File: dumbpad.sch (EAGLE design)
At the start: 44 parts

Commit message: updated readme, made jumpers a little bigger for easier soldering, updated version to 1.0
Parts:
- JP1, JP2: value JUMPER-SMT_3_NO_NO-SILK -> JUMPER-SMT_3_NO_NO_SILK; device SparkFun-Jumpers:JUMPER-SMT_3_NO_NO-SILK -> SparkFun-Jumpers:JUMPER-SMT_3_NO_NO_SILK
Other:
- note added: "Date: April 28, 2020"
- note added: "Rev: 1.0"
- note removed: "Date: April 21, 2020"
- note removed: "Rev: 0.8"
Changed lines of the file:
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@@
 <part name="S17" library="SparkFun-Switches" deviceset="MOMENTARY-SWITCH-SPST" device="-PTH-6.0MM"/>
 <part name="GND4" library="supply1" library_urn="urn:adsk.eagle:library:371" deviceset="GND" device=""/>
-<part name="JP1" library="SparkFun-Jumpers" deviceset="JUMPER-SMT_3_NO" device="_NO-SILK"/>
-<part name="JP2" library="SparkFun-Jumpers" deviceset="JUMPER-SMT_3_NO" device="_NO-SILK"/>
+<part name="JP1" library="SparkFun-Jumpers" deviceset="JUMPER-SMT_3_NO" device="_NO_SILK" value="JUMPER-SMT_3_NO_NO_SILK"/>
+<part name="JP2" library="SparkFun-Jumpers" deviceset="JUMPER-SMT_3_NO" device="_NO_SILK" value="JUMPER-SMT_3_NO_NO_SILK"/>
 <part name="D20" library="SparkFun-LED" deviceset="LED" device="3MM"/>
 <part name="R3" library="SparkFun-Resistors" deviceset="330OHM" device="-HORIZ-1/10W-5%" value="330"/>
@@
 <wire x1="0" y1="172.72" x2="0" y2="0" width="0.1524" layer="97"/>
 <text x="307.34" y="2.54" size="1.778" layer="97">Rev:
-0.8</text>
+1.0</text>
 <text x="279.4" y="2.54" size="1.778" layer="97">Date:
-April 21, 2020</text>
+April 28, 2020</text>
 <text x="279.4" y="10.16" size="1.778" layer="97">Design By:
 github.com/imchipwood</text>

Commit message: swapped some LED pins to make the first two LEDs connecting to the same pins as v0.x PCBs
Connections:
- net LED0: now also B1.12(MISO); no longer B1.13(SCK)
- net LED1: now also B1.13(SCK); no longer B1.12(MISO)
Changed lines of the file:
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@@
 </segment>
 <segment>
-<pinref part="B1" gate="G$1" pin="13(SCK)"/>
-<wire x1="294.64" y1="132.08" x2="302.26" y2="132.08" width="0.1524" layer="91"/>
-<label x="302.26" y="132.08" size="1.778" layer="95"/>
+<pinref part="B1" gate="G$1" pin="12(MISO)"/>
+<wire x1="294.64" y1="129.54" x2="302.26" y2="129.54" width="0.1524" layer="91"/>
+<label x="302.26" y="129.54" size="1.778" layer="95"/>
 </segment>
 </net>
@@
 </segment>
 <segment>
-<pinref part="B1" gate="G$1" pin="12(MISO)"/>
-<wire x1="294.64" y1="129.54" x2="302.26" y2="129.54" width="0.1524" layer="91"/>
-<label x="302.26" y="129.54" size="1.778" layer="95"/>
+<pinref part="B1" gate="G$1" pin="13(SCK)"/>
+<wire x1="294.64" y1="132.08" x2="302.26" y2="132.08" width="0.1524" layer="91"/>
+<label x="302.26" y="132.08" size="1.778" layer="95"/>
 </segment>
 </net>

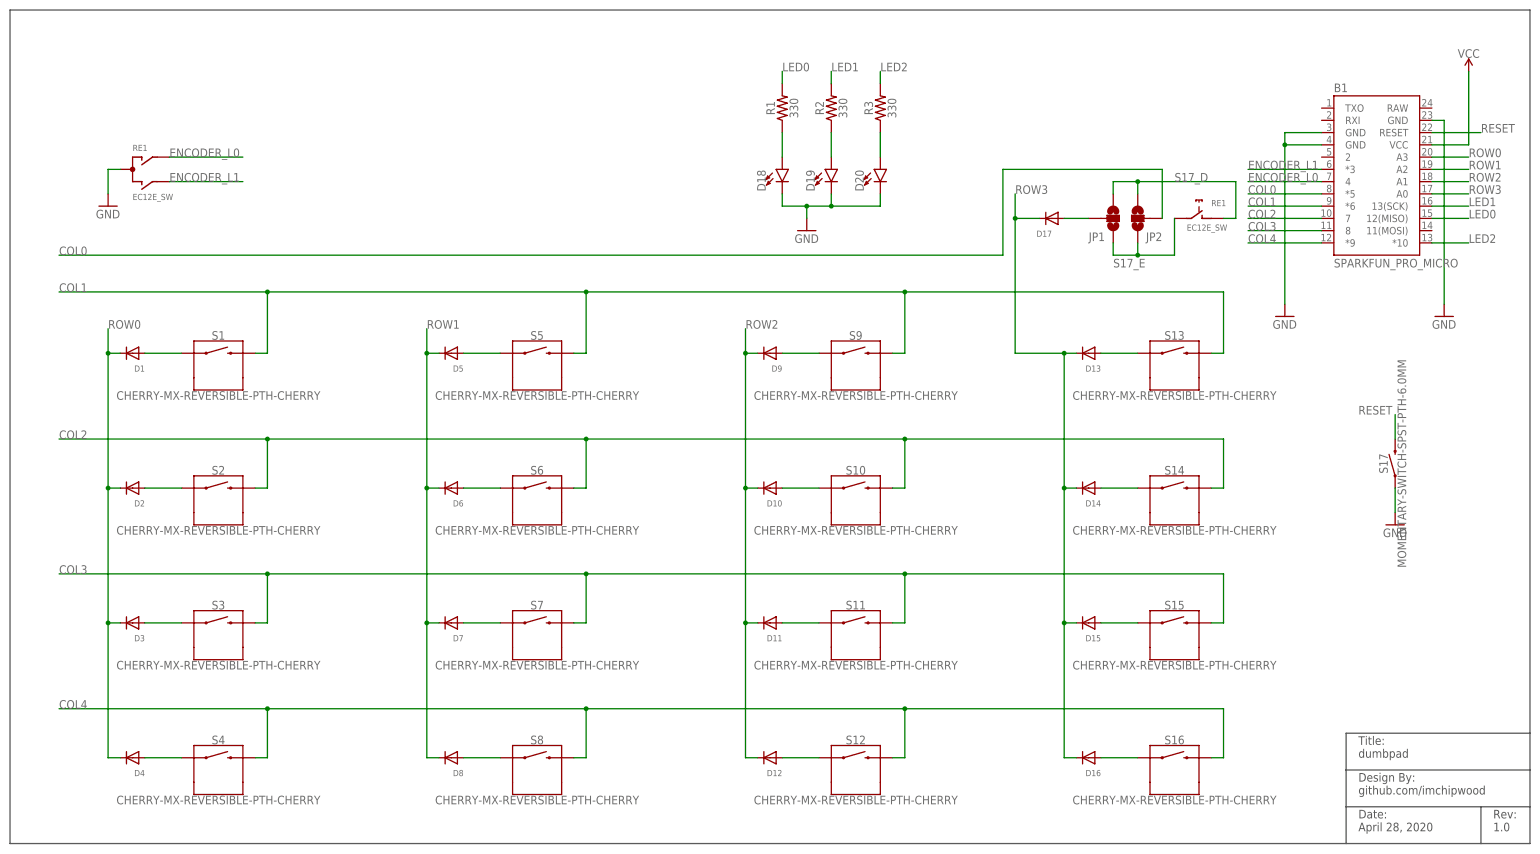
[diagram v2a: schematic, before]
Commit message: all parts have bottom silk screen now, rerouted some stuff
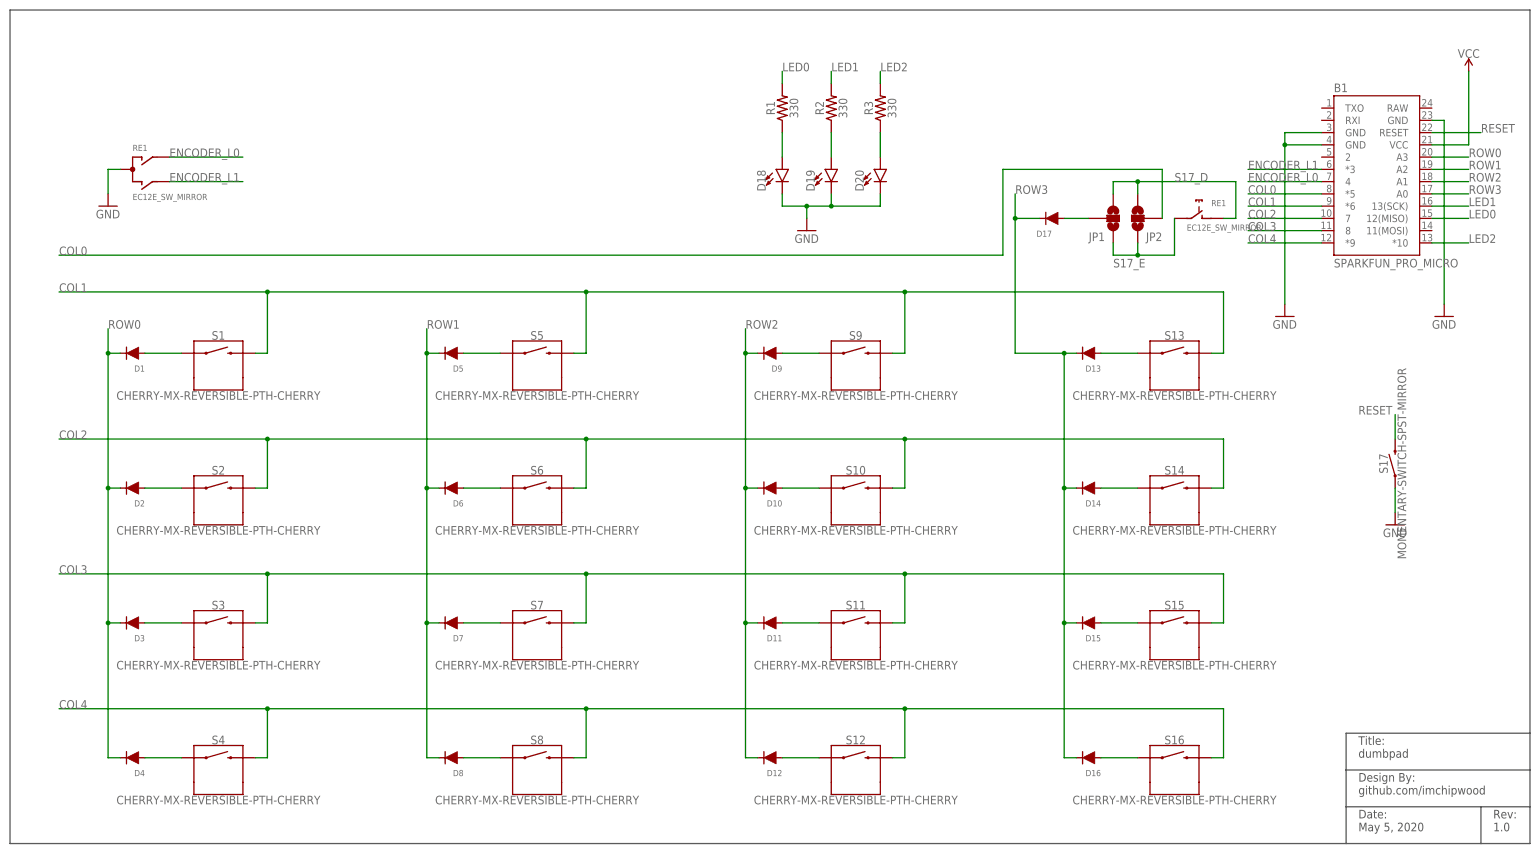
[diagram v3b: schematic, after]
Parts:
- D1, D10, D11, D12, D13, D14, D15, D16, D17, D2, D3, D4, D5, D6, D7, D8, D9: value (none) -> DO-1N4148_MIRROR; device adafruit:DIODEDO-1N4148 -> cpwood:DO-1N4148_MIRROR
- JP1: device SparkFun-Jumpers:JUMPER-SMT_3_NO_NO_SILK -> cpwood:JUMPER-SMT_3_NO_NO_SILK
- R1, R2, R3: device SparkFun-Resistors:330OHM-HORIZ-1/10W-5% -> cpwood:RESISTOR_MIRROR
- RE1: value EC12E_SW -> EC12E_SW_MIRROR; device switch-alps:EC12E_SW -> cpwood:EC12E_SW_MIRROR
- S17: value MOMENTARY-SWITCH-SPST-PTH-6.0MM -> MOMENTARY-SWITCH-SPST-MIRROR; device SparkFun-Switches:MOMENTARY-SWITCH-SPST-PTH-6.0MM -> cpwood:MOMENTARY-SWITCH-SPST-MIRROR
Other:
- note added: "Date: May 5, 2020"
- note removed: "Date: April 28, 2020"
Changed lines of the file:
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@@
 <part name="S1" library="cpwood" deviceset="CHERRY-MX-REVERSIBLE" device="-PTH-CHERRY"/>
 <part name="B1" library="SparkFun-Boards" deviceset="SPARKFUN_PRO_MICRO" device=""/>
-<part name="RE1" library="switch-alps" library_urn="urn:adsk.eagle:library:373" deviceset="EC12E_SW" device="" package3d_urn="urn:adsk.eagle:package:27083/1"/>
+<part name="RE1" library="cpwood" deviceset="EC12E_SW_MIRROR" device="" package3d_urn="urn:adsk.eagle:package:27083/1"/>
 <part name="GND1" library="supply1" library_urn="urn:adsk.eagle:library:371" deviceset="GND" device=""/>
 <part name="S2" library="cpwood" deviceset="CHERRY-MX-REVERSIBLE" device="-PTH-CHERRY"/>
@@
 <part name="GND3" library="supply1" library_urn="urn:adsk.eagle:library:371" deviceset="GND" device=""/>
 <part name="SUPPLY2" library="SparkFun-PowerSymbols" deviceset="VCC" device=""/>
-<part name="D1" library="adafruit" deviceset="DIODE" device="DO-1N4148"/>
-<part name="D2" library="adafruit" deviceset="DIODE" device="DO-1N4148"/>
-<part name="D3" library="adafruit" deviceset="DIODE" device="DO-1N4148"/>
-<part name="D4" library="adafruit" deviceset="DIODE" device="DO-1N4148"/>
-<part name="D5" library="adafruit" deviceset="DIODE" device="DO-1N4148"/>
-<part name="D6" library="adafruit" deviceset="DIODE" device="DO-1N4148"/>
-<part name="D7" library="adafruit" deviceset="DIODE" device="DO-1N4148"/>
-<part name="D8" library="adafruit" deviceset="DIODE" device="DO-1N4148"/>
-<part name="D9" library="adafruit" deviceset="DIODE" device="DO-1N4148"/>
-<part name="D10" library="adafruit" deviceset="DIODE" device="DO-1N4148"/>
-<part name="D11" library="adafruit" deviceset="DIODE" device="DO-1N4148"/>
-<part name="D12" library="adafruit" deviceset="DIODE" device="DO-1N4148"/>
-<part name="D13" library="adafruit" deviceset="DIODE" device="DO-1N4148"/>
-<part name="D14" library="adafruit" deviceset="DIODE" device="DO-1N4148"/>
-<part name="D15" library="adafruit" deviceset="DIODE" device="DO-1N4148"/>
-<part name="D16" library="adafruit" deviceset="DIODE" device="DO-1N4148"/>
-<part name="D17" library="adafruit" deviceset="DIODE" device="DO-1N4148"/>
+<part name="D1" library="cpwood" deviceset="DO-1N4148_MIRROR" device=""/>
+<part name="D2" library="cpwood" deviceset="DO-1N4148_MIRROR" device=""/>
+<part name="D3" library="cpwood" deviceset="DO-1N4148_MIRROR" device=""/>
+<part name="D4" library="cpwood" deviceset="DO-1N4148_MIRROR" device=""/>
+<part name="D5" library="cpwood" deviceset="DO-1N4148_MIRROR" device=""/>
+<part name="D6" library="cpwood" deviceset="DO-1N4148_MIRROR" device=""/>
+<part name="D7" library="cpwood" deviceset="DO-1N4148_MIRROR" device=""/>
+<part name="D8" library="cpwood" deviceset="DO-1N4148_MIRROR" device=""/>
+<part name="D9" library="cpwood" deviceset="DO-1N4148_MIRROR" device=""/>
+<part name="D10" library="cpwood" deviceset="DO-1N4148_MIRROR" device=""/>
+<part name="D11" library="cpwood" deviceset="DO-1N4148_MIRROR" device=""/>
+<part name="D12" library="cpwood" deviceset="DO-1N4148_MIRROR" device=""/>
+<part name="D13" library="cpwood" deviceset="DO-1N4148_MIRROR" device=""/>
+<part name="D14" library="cpwood" deviceset="DO-1N4148_MIRROR" device=""/>
+<part name="D15" library="cpwood" deviceset="DO-1N4148_MIRROR" device=""/>
+<part name="D16" library="cpwood" deviceset="DO-1N4148_MIRROR" device=""/>
+<part name="D17" library="cpwood" deviceset="DO-1N4148_MIRROR" device=""/>
 <part name="D18" library="SparkFun-LED" deviceset="LED" device="3MM"/>
 <part name="D19" library="SparkFun-LED" deviceset="LED" device="3MM"/>
-<part name="R1" library="SparkFun-Resistors" deviceset="330OHM" device="-HORIZ-1/10W-5%" value="330"/>
-<part name="R2" library="SparkFun-Resistors" deviceset="330OHM" device="-HORIZ-1/10W-5%" value="330"/>
+<part name="R1" library="cpwood" deviceset="RESISTOR_MIRROR" device="" value="330"/>
+<part name="R2" library="cpwood" deviceset="RESISTOR_MIRROR" device="" value="330"/>
 <part name="GND2" library="supply1" library_urn="urn:adsk.eagle:library:371" deviceset="GND" device=""/>
-<part name="S17" library="SparkFun-Switches" deviceset="MOMENTARY-SWITCH-SPST" device="-PTH-6.0MM"/>
+<part name="S17" library="cpwood" deviceset="MOMENTARY-SWITCH-SPST-MIRROR" device=""/>
 <part name="GND4" library="supply1" library_urn="urn:adsk.eagle:library:371" deviceset="GND" device=""/>
-<part name="JP1" library="SparkFun-Jumpers" deviceset="JUMPER-SMT_3_NO" device="_NO_SILK" value="JUMPER-SMT_3_NO_NO_SILK"/>
+<part name="JP1" library="cpwood" deviceset="JUMPER-SMT_3_NO" device="_NO_SILK" value="JUMPER-SMT_3_NO_NO_SILK"/>
 <part name="JP2" library="SparkFun-Jumpers" deviceset="JUMPER-SMT_3_NO" device="_NO_SILK" value="JUMPER-SMT_3_NO_NO_SILK"/>
 <part name="D20" library="SparkFun-LED" deviceset="LED" device="3MM"/>
-<part name="R3" library="SparkFun-Resistors" deviceset="330OHM" device="-HORIZ-1/10W-5%" value="330"/>
+<part name="R3" library="cpwood" deviceset="RESISTOR_MIRROR" device="" value="330"/>
 </parts>
 <sheets>
@@
 1.0</text>
 <text x="279.4" y="2.54" size="1.778" layer="97">Date:
-April 28, 2020</text>
+May 5, 2020</text>
 <text x="279.4" y="10.16" size="1.778" layer="97">Design By:
 github.com/imchipwood</text>
@@
 <instance part="D1" gate="G$1" x="25.4" y="101.6" smashed="yes" rot="R180">
 <attribute name="NAME" x="27.94" y="99.06" size="1.27" layer="95" rot="R180"/>
-<attribute name="VALUE" x="27.94" y="105.41" size="1.27" layer="96" rot="R180"/>
 </instance>
 <instance part="D2" gate="G$1" x="25.4" y="73.66" smashed="yes" rot="R180">
 <attribute name="NAME" x="27.94" y="71.12" size="1.27" layer="95" rot="R180"/>
-<attribute name="VALUE" x="27.94" y="77.47" size="1.27" layer="96" rot="R180"/>
 </instance>
 <instance part="D3" gate="G$1" x="25.4" y="45.72" smashed="yes" rot="R180">
 <attribute name="NAME" x="27.94" y="43.18" size="1.27" layer="95" rot="R180"/>
-<attribute name="VALUE" x="27.94" y="49.53" size="1.27" layer="96" rot="R180"/>
 </instance>
 <instance part="D4" gate="G$1" x="25.4" y="17.78" smashed="yes" rot="R180">
 <attribute name="NAME" x="27.94" y="15.24" size="1.27" layer="95" rot="R180"/>
-<attribute name="VALUE" x="27.94" y="21.59" size="1.27" layer="96" rot="R180"/>
 </instance>
 <instance part="D5" gate="G$1" x="91.44" y="101.6" smashed="yes" rot="R180">
 <attribute name="NAME" x="93.98" y="99.06" size="1.27" layer="95" rot="R180"/>
-<attribute name="VALUE" x="93.98" y="105.41" size="1.27" layer="96" rot="R180"/>
 </instance>
 <instance part="D6" gate="G$1" x="91.44" y="73.66" smashed="yes" rot="R180">
 <attribute name="NAME" x="93.98" y="71.12" size="1.27" layer="95" rot="R180"/>
-<attribute name="VALUE" x="93.98" y="77.47" size="1.27" layer="96" rot="R180"/>
 </instance>
 <instance part="D7" gate="G$1" x="91.44" y="45.72" smashed="yes" rot="R180">
 <attribute name="NAME" x="93.98" y="43.18" size="1.27" layer="95" rot="R180"/>
-<attribute name="VALUE" x="93.98" y="49.53" size="1.27" layer="96" rot="R180"/>
 </instance>
 <instance part="D8" gate="G$1" x="91.44" y="17.78" smashed="yes" rot="R180">
 <attribute name="NAME" x="93.98" y="15.24" size="1.27" layer="95" rot="R180"/>
-<attribute name="VALUE" x="93.98" y="21.59" size="1.27" layer="96" rot="R180"/>
 </instance>
 <instance part="D9" gate="G$1" x="157.48" y="101.6" smashed="yes" rot="R180">
 <attribute name="NAME" x="160.02" y="99.06" size="1.27" layer="95" rot="R180"/>
-<attribute name="VALUE" x="160.02" y="105.41" size="1.27" layer="96" rot="R180"/>
 </instance>
 <instance part="D10" gate="G$1" x="157.48" y="73.66" smashed="yes" rot="R180">
 <attribute name="NAME" x="160.02" y="71.12" size="1.27" layer="95" rot="R180"/>
-<attribute name="VALUE" x="160.02" y="77.47" size="1.27" layer="96" rot="R180"/>
 </instance>
 <instance part="D11" gate="G$1" x="157.48" y="45.72" smashed="yes" rot="R180">
 <attribute name="NAME" x="160.02" y="43.18" size="1.27" layer="95" rot="R180"/>
-<attribute name="VALUE" x="160.02" y="49.53" size="1.27" layer="96" rot="R180"/>
 </instance>
 <instance part="D12" gate="G$1" x="157.48" y="17.78" smashed="yes" rot="R180">
 <attribute name="NAME" x="160.02" y="15.24" size="1.27" layer="95" rot="R180"/>
-<attribute name="VALUE" x="160.02" y="21.59" size="1.27" layer="96" rot="R180"/>
 </instance>
 <instance part="D13" gate="G$1" x="223.52" y="101.6" smashed="yes" rot="R180">
 <attribute name="NAME" x="226.06" y="99.06" size="1.27" layer="95" rot="R180"/>
-<attribute name="VALUE" x="226.06" y="105.41" size="1.27" layer="96" rot="R180"/>
 </instance>
 <instance part="D14" gate="G$1" x="223.52" y="73.66" smashed="yes" rot="R180">
 <attribute name="NAME" x="226.06" y="71.12" size="1.27" layer="95" rot="R180"/>
-<attribute name="VALUE" x="226.06" y="77.47" size="1.27" layer="96" rot="R180"/>
 </instance>
 <instance part="D15" gate="G$1" x="223.52" y="45.72" smashed="yes" rot="R180">
 <attribute name="NAME" x="226.06" y="43.18" size="1.27" layer="95" rot="R180"/>
-<attribute name="VALUE" x="226.06" y="49.53" size="1.27" layer="96" rot="R180"/>
 </instance>
 <instance part="D16" gate="G$1" x="223.52" y="17.78" smashed="yes" rot="R180">
 <attribute name="NAME" x="226.06" y="15.24" size="1.27" layer="95" rot="R180"/>
-<attribute name="VALUE" x="226.06" y="21.59" size="1.27" layer="96" rot="R180"/>
 </instance>
 <instance part="D17" gate="G$1" x="215.9" y="129.54" smashed="yes" rot="R180">
 <attribute name="NAME" x="215.9" y="127" size="1.27" layer="95" rot="R180"/>
-<attribute name="VALUE" x="218.44" y="133.35" size="1.27" layer="96" rot="R180"/>
 </instance>
 <instance part="D18" gate="D1" x="160.02" y="139.7" smashed="yes">

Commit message: fixed issue with wrong jumper size
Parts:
- JP2: device SparkFun-Jumpers:JUMPER-SMT_3_NO_NO_SILK -> cpwood:JUMPER-SMT_3_NO_NO_SILK
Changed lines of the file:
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@@
 <part name="GND4" library="supply1" library_urn="urn:adsk.eagle:library:371" deviceset="GND" device=""/>
 <part name="JP1" library="cpwood" deviceset="JUMPER-SMT_3_NO" device="_NO_SILK" value="JUMPER-SMT_3_NO_NO_SILK"/>
-<part name="JP2" library="SparkFun-Jumpers" deviceset="JUMPER-SMT_3_NO" device="_NO_SILK" value="JUMPER-SMT_3_NO_NO_SILK"/>
+<part name="JP2" library="cpwood" deviceset="JUMPER-SMT_3_NO" device="_NO_SILK" value="JUMPER-SMT_3_NO_NO_SILK"/>
 <part name="D20" library="SparkFun-LED" deviceset="LED" device="3MM"/>
 <part name="R3" library="cpwood" deviceset="RESISTOR_MIRROR" device="" value="330"/>
